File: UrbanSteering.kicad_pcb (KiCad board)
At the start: 2 copper layers, 144 x 100 mm, 49 parts, among them J1 Joystick, J2 Main_conn, J3 CAN_term, J4 STM32L432, J5 Screen_Left, J6 Screen_Right, J9 Proximity_sensor, U1 MCP2562, U2 74HC595PW, U3 74HC597D

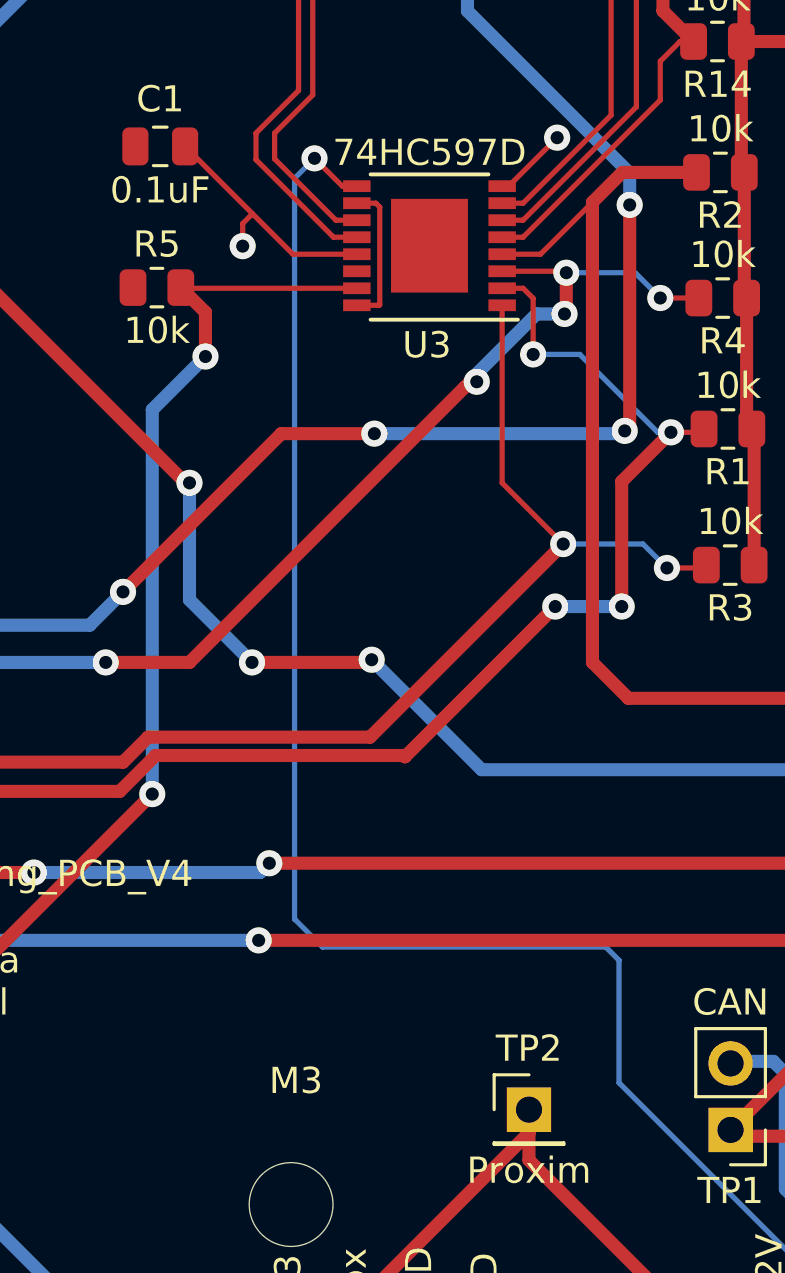
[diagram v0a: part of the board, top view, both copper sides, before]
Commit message: Physical hardware changes replicated in KiCad design
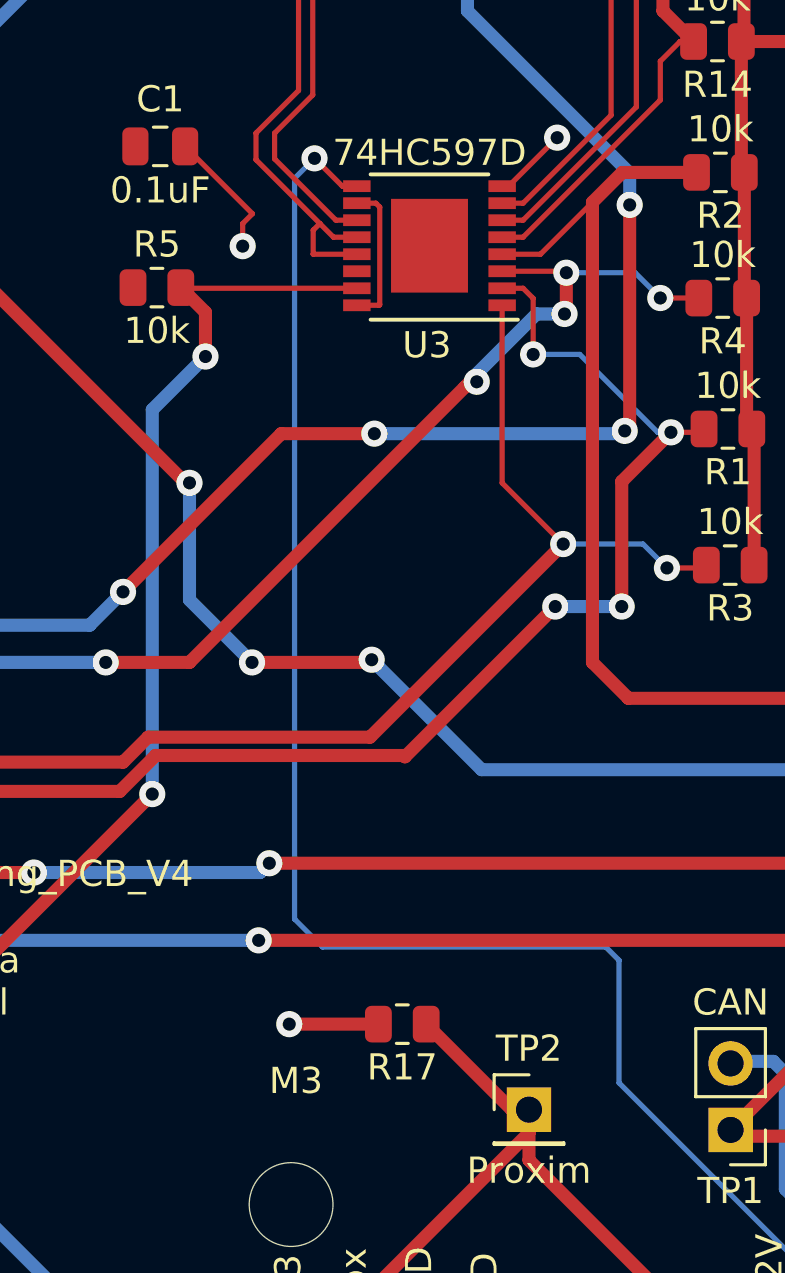
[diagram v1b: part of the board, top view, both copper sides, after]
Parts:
- added R17: 10k, Resistor_SMD:R_0805_2012Metric, F.Cu at (149.2, 113.1)
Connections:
- U3 pad 13: GND -> /Latch
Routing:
- net /ProximInput: track 94.7 -> 100.0 mm
- net /Latch: track 143.4 -> 146.3 mm
- net GND: track 87.9 -> 86.7 mm, vias 5 -> 6
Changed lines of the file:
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@@
   (net 65 "unconnected-(U2-Pad15)")
   (net 66 "unconnected-(U3-Pad14)")
-  (net 67 "Net-(J2-Pad8)")
+  (net 67 "Net-(F1-Pad1)")
   (footprint "schematic:STM32L432" (layer "F.Cu")
     (at 228 139.28 -90)
@@
     (pad "2" smd roundrect (at 0.9125 0 180) (size 1.025 1.4) (layers "F.Cu" "F.Paste" "F.Mask") (roundrect_rratio 0.243902439)
       (net 53 "Net-(R11-Pad2)") (pintype "passive"))
+    (model "${KICAD6_3DMODEL_DIR}/Resistor_SMD.3dshapes/R_0805_2012Metric.wrl"
+      (offset (xyz 0 0 0))
+      (scale (xyz 1 1 1))
+      (rotate (xyz 0 0 0))
+    )
+  )
+  (footprint "Resistor_SMD:R_0805_2012Metric" (layer "F.Cu")
+    (at 149.246779 113.10874 180)
+    (descr "Resistor SMD 0805 (2012 Metric), square (rectangular) end terminal, IPC_7351 nominal, (Body size source: IPC-SM-782 page 72, https://www.pcb-3d.com/wordpress/wp-content/uploads/ipc-sm-782a_amendment_1_and_2.pdf), generated with kicad-footprint-generator")
+    (tags "resistor")
+    (property "Sheetfile" "UrbanSteering.kicad_sch")
+    (property "Sheetname" "")
+    (attr smd)
+    (fp_text reference "R17" (at 0 -1.65) (layer "F.SilkS")
+      (effects (font (size 1 1) (thickness 0.15)))
+    )
+    (fp_text value "10k" (at 0 1.65) (layer "F.Fab")
+      (effects (font (size 1 1) (thickness 0.15)))
+    )
+    (fp_text user "${REFERENCE}" (at 0 0) (layer "F.Fab")
+      (effects (font (size 0.5 0.5) (thickness 0.08)))
+    )
+    (fp_line (start -0.227064 -0.735) (end 0.227064 -0.735) (layer "F.SilkS") (width 0.12))
+    (fp_line (start -0.227064 0.735) (end 0.227064 0.735) (layer "F.SilkS") (width 0.12))
+    (fp_line (start 1.68 -0.95) (end 1.68 0.95) (layer "F.CrtYd") (width 0.05))
+    (fp_line (start 1.68 0.95) (end -1.68 0.95) (layer "F.CrtYd") (width 0.05))
+    (fp_line (start -1.68 -0.95) (end 1.68 -0.95) (layer "F.CrtYd") (width 0.05))
+    (fp_line (start -1.68 0.95) (end -1.68 -0.95) (layer "F.CrtYd") (width 0.05))
+    (fp_line (start -1 0.625) (end -1 -0.625) (layer "F.Fab") (width 0.1))
+    (fp_line (start -1 -0.625) (end 1 -0.625) (layer "F.Fab") (width 0.1))
+    (fp_line (start 1 -0.625) (end 1 0.625) (layer "F.Fab") (width 0.1))
+    (fp_line (start 1 0.625) (end -1 0.625) (layer "F.Fab") (width 0.1))
+    (pad "1" smd roundrect (at -0.9125 0 180) (size 1.025 1.4) (layers "F.Cu" "F.Paste" "F.Mask") (roundrect_rratio 0.243902)
+      (net 29 "/ProximInput") (pintype "passive"))
+    (pad "2" smd roundrect (at 0.9125 0 180) (size 1.025 1.4) (layers "F.Cu" "F.Paste" "F.Mask") (roundrect_rratio 0.243902)
+      (net 1 "GND") (pintype "passive"))
     (model "${KICAD6_3DMODEL_DIR}/Resistor_SMD.3dshapes/R_0805_2012Metric.wrl"
       (offset (xyz 0 0 0))
@@
       (net 18 "/Latch") (pinfunction "STCP") (pintype "input"))
     (pad "13" smd rect (at 2.775 -0.325 180) (size 1.05 0.45) (layers "F.Cu" "F.Paste" "F.Mask")
-      (net 1 "GND") (pinfunction "PL*") (pintype "input"))
+      (net 18 "/Latch") (pinfunction "PL*") (pintype "input"))
     (pad "14" smd rect (at 2.775 -0.975 180) (size 1.05 0.45) (layers "F.Cu" "F.Paste" "F.Mask")
       (net 66 "unconnected-(U3-Pad14)") (pinfunction "DS") (pintype "input+no_connect"))
@@
       (net 1 "GND") (pinfunction "Pin_7") (pintype "passive"))
     (pad "8" thru_hole circle (at 17.78 0 180) (size 1.635 1.635) (drill 1.09) (layers *.Cu *.Mask)
-      (net 67 "Net-(J2-Pad8)") (pinfunction "Pin_8") (pintype "passive"))
+      (net 67 "Net-(F1-Pad1)") (pinfunction "Pin_8") (pintype "passive"))
     (model "70551-0007.stp"
       (offset (xyz 8.89000021 7.110000027 2.880000071))
@@
     (fp_line (start 1.6 -0.8) (end 1.6 0.8) (layer "F.Fab") (width 0.1))
     (pad "1" smd roundrect (at -1.4 0) (size 1.25 1.75) (layers "F.Cu" "F.Paste" "F.Mask") (roundrect_rratio 0.2)
-      (net 67 "Net-(J2-Pad8)") (pintype "passive"))
+      (net 67 "Net-(F1-Pad1)") (pintype "passive"))
     (pad "2" smd roundrect (at 1.4 0) (size 1.25 1.75) (layers "F.Cu" "F.Paste" "F.Mask") (roundrect_rratio 0.2)
       (net 2 "+12V") (pintype "passive"))
@@
   (segment (start 162.298479 72.77744) (end 162.298479 75.47474) (width 0.5) (layer "F.Cu") (net 1))
   (segment (start 162.598479 90.37474) (end 162.685979 90.46224) (width 0.5) (layer "F.Cu") (net 1))
-  (segment (start 145.070179 83.69974) (end 143.524179 82.15374) (width 0.2) (layer "F.Cu") (net 1))
   (segment (start 162.310979 85.28724) (end 162.398479 85.37474) (width 0.5) (layer "F.Cu") (net 1))
   (segment (start 143.524179 82.15374) (end 140.951179 79.58074) (width 0.2) (layer "F.Cu") (net 1))
@@
   (segment (start 143.150779 82.52714) (end 143.150779 83.39074) (width 0.2) (layer "F.Cu") (net 1))
   (segment (start 162.398479 90.17474) (end 162.598479 90.37474) (width 0.5) (layer "F.Cu") (net 1))
-  (segment (start 147.510979 83.69974) (end 145.070179 83.69974) (width 0.2) (layer "F.Cu") (net 1))
   (segment (start 153.060979 81.09974) (end 153.309603 81.09974) (width 0.2) (layer "F.Cu") (net 1))
   (segment (start 162.198479 80.46224) (end 162.198479 75.57474) (width 0.5) (layer "F.Cu") (net 1))
+  (segment (start 148.334279 113.10874) (end 144.928779 113.10874) (width 0.5) (layer "F.Cu") (net 1))
   (segment (start 168.960979 67.89974) (end 168.285979 67.22474) (width 0.2) (layer "F.Cu") (net 1))
   (via (at 185.213179 109.04474) (size 1) (drill 0.5) (layers "F.Cu" "B.Cu") (net 1))
@@
   (via (at 165.385979 75.67474) (size 1) (drill 0.5) (layers "F.Cu" "B.Cu") (net 1))
   (via (at 201.265979 85.93074) (size 1) (drill 0.5) (layers "F.Cu" "B.Cu") (net 1))
+  (via (at 144.928779 113.10874) (size 1) (drill 0.5) (layers "F.Cu" "B.Cu") (net 1))
   (via (at 143.150779 83.39074) (size 1) (drill 0.5) (layers "F.Cu" "B.Cu") (net 1))
   (segment (start 188.793979 115.67474) (end 191.685979 115.67474) (width 0.5) (layer "F.Cu") (net 2))
@@
   (segment (start 203.196379 89.08034) (end 208.835179 94.71914) (width 0.2) (layer "B.Cu") (net 17))
   (segment (start 228.494779 135.61314) (end 228.545579 135.66394) (width 0.5) (layer "B.Cu") (net 17))
+  (segment (start 145.843179 83.69554) (end 145.847379 83.69974) (width 0.2) (layer "F.Cu") (net 18))
   (segment (start 143.658779 79.07274) (end 145.284379 77.44714) (width 0.2) (layer "F.Cu") (net 18))
   (segment (start 153.07055 59.56554) (end 164.426779 59.56554) (width 0.2) (layer "F.Cu") (net 18))
   (segment (start 191.466025 106.153586) (end 191.923225 106.153586) (width 0.2) (layer "F.Cu") (net 18))
-  (segment (start 146.619779 83.04974) (end 143.658779 80.08874) (width 0.2) (layer "F.Cu") (net 18))
   (segment (start 164.426779 59.56554) (end 172.110979 67.24974) (width 0.2) (layer "F.Cu") (net 18))
   (segment (start 145.284379 77.44714) (end 145.284379 67.351711) (width 0.2) (layer "F.Cu") (net 18))
   (segment (start 147.510979 83.04974) (end 146.619779 83.04974) (width 0.2) (layer "F.Cu") (net 18))
   (segment (start 207.260379 119.05234) (end 207.260379 122.57524) (width 0.2) (layer "F.Cu") (net 18))
+  (segment (start 145.847379 83.69974) (end 147.510979 83.69974) (width 0.2) (layer "F.Cu") (net 18))
   (segment (start 216.57 131.054361) (end 215.489979 129.97434) (width 0.5) (layer "F.Cu") (net 18))
   (segment (start 145.284379 67.351711) (end 153.07055 59.56554) (width 0.2) (layer "F.Cu") (net 18))
@@
   (segment (start 170.985479 67.24974) (end 170.785979 67.05024) (width 0.2) (layer "F.Cu") (net 18))
   (segment (start 184.287348 87.900509) (end 184.287348 87.964525) (width 0.2) (layer "F.Cu") (net 18))
+  (segment (start 146.097179 82.52714) (end 145.843179 82.78114) (width 0.2) (layer "F.Cu") (net 18))
   (segment (start 172.910979 67.24974) (end 170.985479 67.24974) (width 0.2) (layer "F.Cu") (net 18))
   (segment (start 172.110979 67.24974) (end 172.910979 67.24974) (width 0.2) (layer "F.Cu") (net 18))
+  (segment (start 146.097179 82.52714) (end 143.658779 80.08874) (width 0.2) (layer "F.Cu") (net 18))
   (segment (start 216.57 131.66) (end 216.57 131.054361) (width 0.5) (layer "F.Cu") (net 18))
+  (segment (start 145.843179 82.78114) (end 145.843179 83.69554) (width 0.2) (layer "F.Cu") (net 18))
   (segment (start 186.127579 100.81514) (end 191.466025 106.153586) (width 0.2) (layer "F.Cu") (net 18))
+  (segment (start 146.619779 83.04974) (end 146.097179 82.52714) (width 0.2) (layer "F.Cu") (net 18))
   (segment (start 181.149179 84.76234) (end 184.287348 87.900509) (width 0.2) (layer "F.Cu") (net 18))
   (segment (start 143.658779 80.08874) (end 143.658779 79.07274) (width 0.2) (layer "F.Cu") (net 18))
@@
   (segment (start 214.15 73.7) (end 219.909579 79.459579) (width 0.5) (layer "B.Cu") (net 28))
   (segment (start 147.42 126) (end 147.42 123.927119) (width 0.5) (layer "F.Cu") (net 29))
+  (segment (start 154.085979 116.37474) (end 153.425279 116.37474) (width 0.5) (layer "F.Cu") (net 29))
   (segment (start 154.085979 118.30354) (end 154.085979 116.37474) (width 0.5) (layer "F.Cu") (net 29))
   (segment (start 196.643179 142.57274) (end 196.592379 142.62354) (width 0.5) (layer "F.Cu") (net 29))
@@
   (segment (start 186.991179 136.78154) (end 186.991179 136.07034) (width 0.5) (layer "F.Cu") (net 29))
   (segment (start 187.346779 132.36194) (end 185.162379 130.17754) (width 0.5) (layer "F.Cu") (net 29))
+  (segment (start 153.425279 116.37474) (end 150.159279 113.10874) (width 0.5) (layer "F.Cu") (net 29))
   (via (at 190.851979 140.64234) (size 1) (drill 0.5) (layers "F.Cu" "B.Cu") (net 29))
   (via (at 186.991179 136.07034) (size 1) (drill 0.5) (layers "F.Cu" "B.Cu") (net 29))
